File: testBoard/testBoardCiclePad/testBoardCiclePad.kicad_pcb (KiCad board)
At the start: 2 copper layers, 1 part

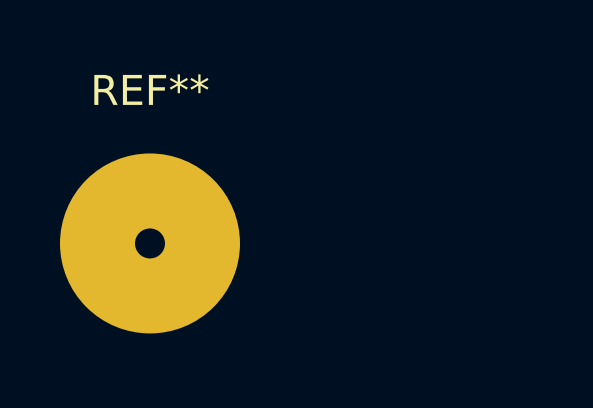
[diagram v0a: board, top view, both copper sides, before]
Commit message: Absolute and relation coordinates in soft parser G-code.
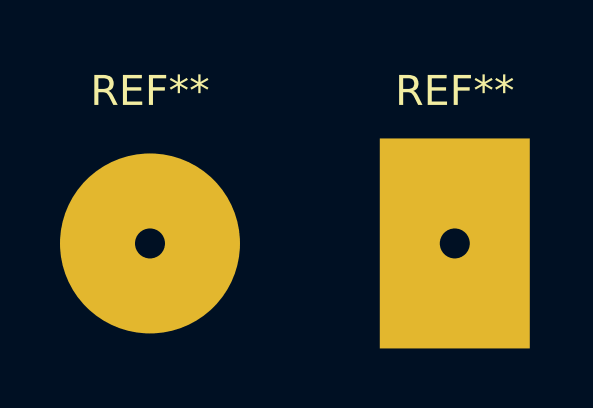
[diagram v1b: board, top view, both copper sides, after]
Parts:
- added REF**: SolderWirePad_1x01_Drill2.5mm, Connector_Wire:SolderWirePad_1x01_Drill2.5mm, F.Cu at (85.1, 45.7)
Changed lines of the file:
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@@
     (tracks 0)
     (zones 0)
-    (modules 1)
+    (modules 2)
     (nets 1)
   )
@@
     (mod_text_size 1 1)
     (mod_text_width 0.15)
-    (pad_size 5.99948 5.99948)
+    (pad_size 5 7)
     (pad_drill 1)
     (pad_to_mask_clearance 0.051)
     (solder_mask_min_width 0.25)
     (aux_axis_origin 0 0)
-    (visible_elements FFFFFF7F)
+    (visible_elements 7FFFFFFF)
     (pcbplotparams
       (layerselection 0x00000_7fffffff)
@@
       (drillshape 0)
       (scaleselection 1)
-      (outputdirectory ""))
+      (outputdirectory "D:/Projects/pbMashine/testBoard/testBoardCiclePad/"))
   )
   (net 0 "")
@@
   )
   (module Connector_Wire:SolderWirePad_1x01_Drill2.5mm (layer F.Cu)
+    (at 85.09 45.72)
+    (descr "Wire solder connection")
+    (tags connector)
+    (attr virtual)
+    (fp_text reference REF** (at 0 -5.08) (layer F.SilkS)
+      (effects (font (size 1 1) (thickness 0.15)))
+    )
+    (fp_text value SolderWirePad_1x01_Drill2.5mm (at 0 5.08) (layer F.Fab)
+      (effects (font (size 1 1) (thickness 0.15)))
+    )
+    (fp_text user %R (at 0 0) (layer F.Fab)
+      (effects (font (size 1 1) (thickness 0.15)))
+    )
+    (fp_line (start -3.5 -3.5) (end 3.5 -3.5) (layer F.CrtYd) (width 0.05))
+    (fp_line (start -3.5 -3.5) (end -3.5 3.5) (layer F.CrtYd) (width 0.05))
+    (fp_line (start 3.5 3.5) (end 3.5 -3.5) (layer F.CrtYd) (width 0.05))
+    (fp_line (start 3.5 3.5) (end -3.5 3.5) (layer F.CrtYd) (width 0.05))
+    (pad 1 thru_hole rect (at 0 0) (size 5 7) (drill 1) (layers *.Cu *.Mask))
+  )
+  (module Connector_Wire:SolderWirePad_1x01_Drill2.5mm (layer F.Cu)

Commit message: Start fixing oval pad.
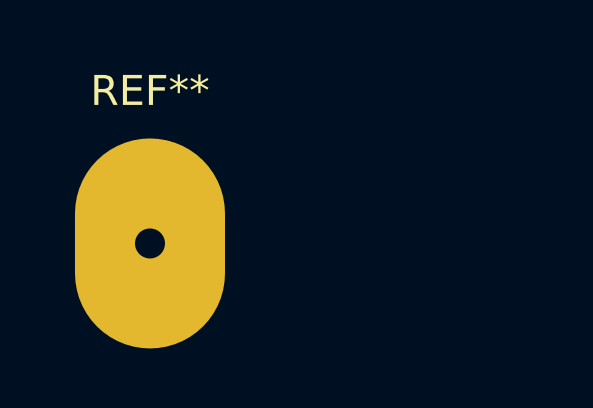
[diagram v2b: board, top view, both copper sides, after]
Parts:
- removed the REF** at (85.1, 45.7)
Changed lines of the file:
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@@
     (tracks 0)
     (zones 0)
-    (modules 2)
+    (modules 1)
     (nets 1)
   )
@@
   )
   (module Connector_Wire:SolderWirePad_1x01_Drill2.5mm (layer F.Cu)
-    (at 85.09 45.72)
-    (descr "Wire solder connection")
-    (tags connector)
-    (attr virtual)
-    (fp_text reference REF** (at 0 -5.08) (layer F.SilkS)
-      (effects (font (size 1 1) (thickness 0.15)))
-    )
-    (fp_text value SolderWirePad_1x01_Drill2.5mm (at 0 5.08) (layer F.Fab)
-      (effects (font (size 1 1) (thickness 0.15)))
-    )
-    (fp_text user %R (at 0 0) (layer F.Fab)
-      (effects (font (size 1 1) (thickness 0.15)))
-    )
-    (fp_line (start -3.5 -3.5) (end 3.5 -3.5) (layer F.CrtYd) (width 0.05))
-    (fp_line (start -3.5 -3.5) (end -3.5 3.5) (layer F.CrtYd) (width 0.05))
-    (fp_line (start 3.5 3.5) (end 3.5 -3.5) (layer F.CrtYd) (width 0.05))
-    (fp_line (start 3.5 3.5) (end -3.5 3.5) (layer F.CrtYd) (width 0.05))
-    (pad 1 thru_hole rect (at 0 0) (size 5 7) (drill 1) (layers *.Cu *.Mask))
-  )
-  (module Connector_Wire:SolderWirePad_1x01_Drill2.5mm (layer F.Cu)
     (at 74.93 45.72)
     (descr "Wire solder connection")
@@
       (effects (font (size 1 1) (thickness 0.15)))
     )
-    (pad 1 thru_hole circle (at 0 0) (size 5.99948 5.99948) (drill 1) (layers *.Cu *.Mask))
+    (pad 1 thru_hole oval (at 0 0) (size 5 7) (drill 1) (layers *.Cu *.Mask))
   )
 )
